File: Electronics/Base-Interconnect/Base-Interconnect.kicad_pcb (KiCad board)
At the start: 2 copper layers, 0 parts

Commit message: Base interconnect and head interconnect in fabrication
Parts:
- added H1: MountingHole_Pad, MountingHole:MountingHole_3.2mm_M3_Pad_Via, F.Cu at (161.7, 45.2)
- added H2: MountingHole_Pad, MountingHole:MountingHole_3.2mm_M3_Pad_Via, F.Cu at (197.8, 48.4)
- added H3: MountingHole_Pad, MountingHole:MountingHole_3.2mm_M3_Pad_Via, F.Cu at (218.6, 84.4)
- added H4: MountingHole_Pad, MountingHole:MountingHole_3.2mm_M3_Pad_Via, F.Cu at (203.3, 117.2)
- added J1: DB9_Male_MountingHoles, STM_Custom_Lib:DSUB-9_Amphenol_LD09S33E4GV00LF-Center, F.Cu at (181.7, 34.0)
- added J2: DB9_Male_MountingHoles, STM_Custom_Lib:DSUB-9_Amphenol_LD09S33E4GV00LF-Center, F.Cu at (213.5, 63.4)
- added J3: DB9_Male_MountingHoles, STM_Custom_Lib:DSUB-9_Amphenol_LD09S33E4GV00LF-Center, F.Cu at (223.1, 105.5)
- added J4: Conn_01x20, STM_Custom_Lib:molex_0526102072, F.Cu at (206.3, 100.6)
- added REF**: OSHW-Symbol_6.7x6mm_SilkScreen, Symbol:OSHW-Symbol_6.7x6mm_SilkScreen, F.Cu at (175.0, 49.0)
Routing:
- net /stepper_A+: track 0.00 -> 76.1 mm, vias 0 -> 1
- net /stepper_A-: track 0.00 -> 74.5 mm, vias 0 -> 1
- net /stepper_B-: track 0.00 -> 72.0 mm, vias 0 -> 1
- net /stepper_B+: track 0.00 -> 71.5 mm, vias 0 -> 1
- net /tunnel_gnd: track 0.00 -> 55.0 mm, vias 0 -> 1
- net /analog_+15V: track 0.00 -> 49.5 mm
- net /tunnel_signal: track 0.00 -> 43.9 mm, vias 0 -> 1
- net /analog_-15V: track 0.00 -> 43.0 mm, vias 0 -> 1
- net /bias: track 0.00 -> 36.6 mm
- net /analog_gnd: track 0.00 -> 23.1 mm, vias 0 -> 19
- net /piezo_y+: track 0.00 -> 19.9 mm, vias 0 -> 1
- net /piezo_x+: track 0.00 -> 19.1 mm, vias 0 -> 1
- net /piezo_x-: track 0.00 -> 13.9 mm
- net /piezo_y-: track 0.00 -> 10.9 mm
- added copper zone on B.Cu, net /analog_gnd
- added copper zone on F.Cu, net /analog_gnd
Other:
- board outline added: 66.5 x 101.6 mm
- board text added: "STM Base Interconnect V1"
- board text added: "©mrkenhoff 2020"

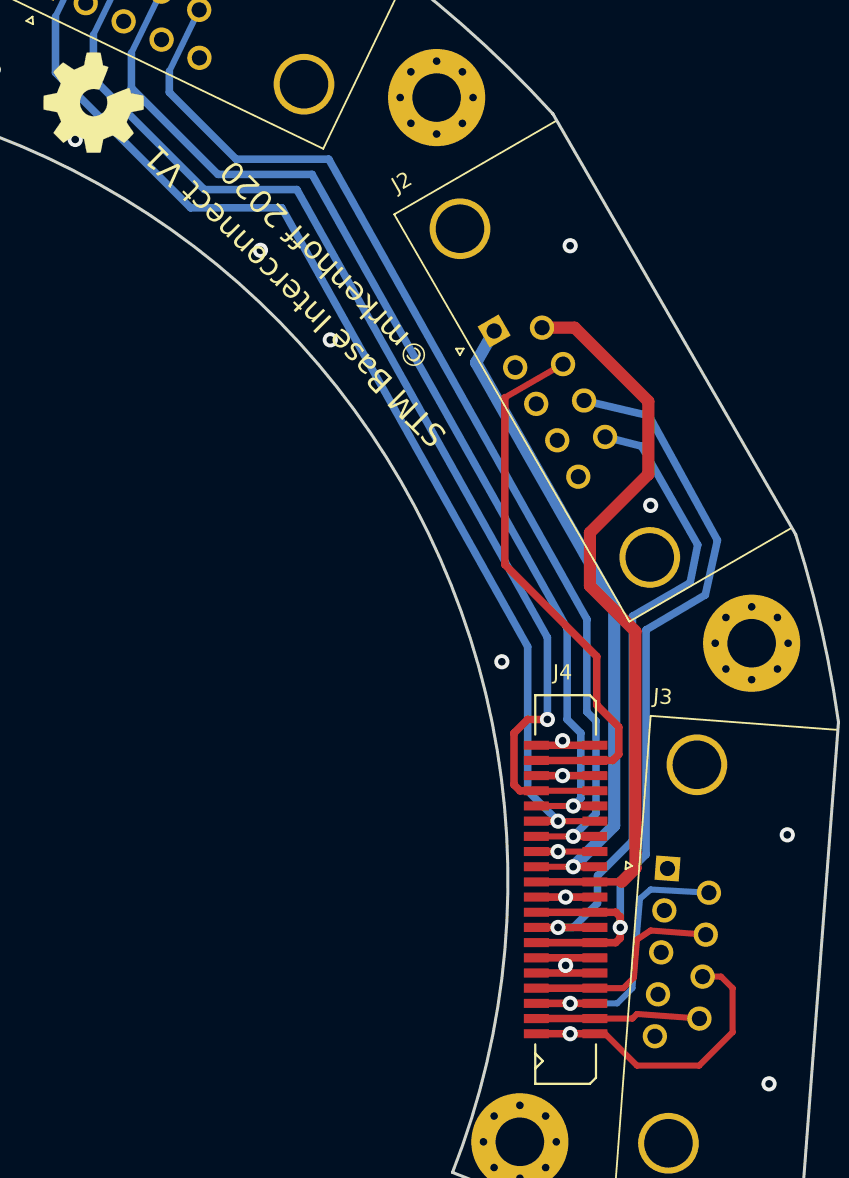
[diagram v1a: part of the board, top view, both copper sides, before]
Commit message: Added sample-bias interconnect and base interconnect V2
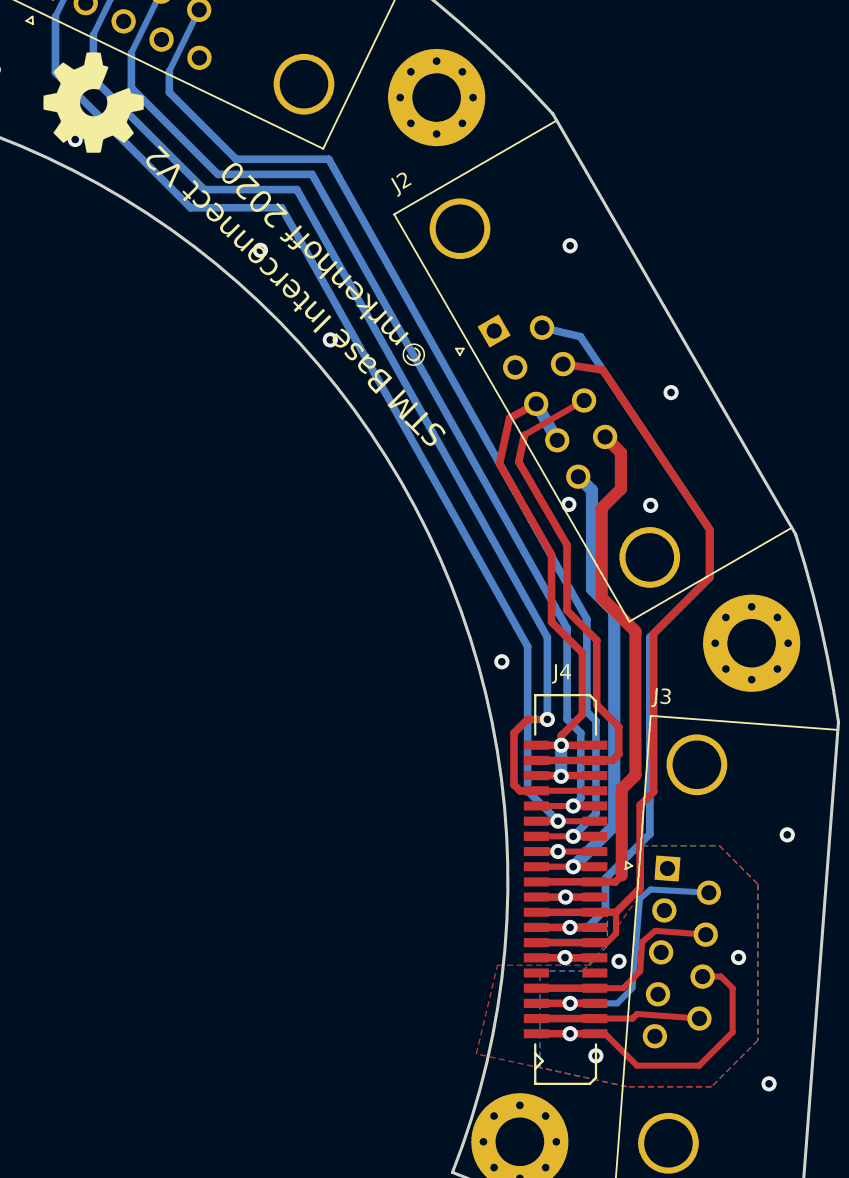
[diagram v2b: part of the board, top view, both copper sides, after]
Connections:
- J1 pad 1: /stepper_shield -> Net-(J1-Pad1)
- J1 pad 2: /stepper_shield -> Net-(J1-Pad2)
- J1 pad 3: /stepper_shield -> Net-(J1-Pad3)
- J1 pad 4: /stepper_shield -> Net-(J1-Pad4)
- J1 pad 5: /stepper_shield -> Net-(J1-Pad5)
- J1 pad 6: /stepper_A+ -> /stepper_B-
- J1 pad 7: /stepper_A- -> /stepper_B+
- J1 pad 8: /stepper_B+ -> /stepper_A-
- J1 pad 9: /stepper_B- -> /stepper_A+
- J2 pad 1: /analog_-15V -> /analog_gnd
- J2 pad 3: /analog_gnd -> /bias_gnd
- J2 pad 4: /analog_gnd -> /bias_gnd
- J2 pad 5: /analog_gnd -> /analog_-15V
- J2 pad 6: /analog_+15V -> /tunnel_signal
- J2 pad 7: /bias -> /tunnel_gnd
- J2 pad 8: /tunnel_gnd -> /bias
- J2 pad 9: /tunnel_signal -> /analog_+15V
- J3 pad 1: /analog_gnd -> /piezo_gnd
- J3 pad 2: /analog_gnd -> /piezo_gnd
- J3 pad 3: /analog_gnd -> /piezo_gnd
- J3 pad 4: /analog_gnd -> /piezo_gnd
- J3 pad 5: /analog_gnd -> /piezo_gnd
- J3 pad 6: /piezo_x+ -> /piezo_y-
- J3 pad 7: /piezo_x- -> /piezo_y+
- J3 pad 8: /piezo_y+ -> /piezo_x-
- J3 pad 9: /piezo_y- -> /piezo_x+
- J4 pad 1: /piezo_y+ -> /piezo_x-
- J4 pad 14: /stepper_B- -> /stepper_A+
- J4 pad 15: /stepper_A+ -> /stepper_B-
- J4 pad 16: /stepper_B+ -> /stepper_A-
- J4 pad 17: /stepper_A- -> /stepper_B+
- J4 pad 18: /analog_gnd -> /bias_gnd
- J4 pad 2: /piezo_y- -> /piezo_x+
- J4 pad 20: /analog_gnd -> /bias_gnd
- J4 pad 3: /piezo_x+ -> /piezo_y-
- J4 pad 4: /piezo_x- -> /piezo_y+
- J4 pad 5: /analog_gnd -> /piezo_gnd
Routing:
- net /bias_gnd: track 0.00 -> 38.5 mm, vias 0 -> 2
- net /analog_+15V: track 49.5 -> 36.9 mm
- net /analog_gnd: track 23.1 -> 11.5 mm
- net /analog_-15V: track 43.0 -> 31.6 mm
- net /tunnel_signal: track 43.9 -> 52.4 mm
- net /piezo_y-: track 10.9 -> 19.1 mm, vias 0 -> 1
- net /piezo_x+: track 19.1 -> 10.9 mm, vias 1 -> 0
- net /piezo_y+: track 19.9 -> 13.7 mm, vias 1 -> 0
- net /piezo_x-: track 13.9 -> 19.9 mm, vias 0 -> 1
- net /stepper_B-: track 72.0 -> 76.1 mm
- net /stepper_A+: track 76.1 -> 72.0 mm
- net /bias: track 36.6 -> 33.5 mm
- net /stepper_B+: track 71.5 -> 74.5 mm
- net /stepper_A-: track 74.5 -> 71.5 mm
- net /tunnel_gnd: track 55.0 -> 55.2 mm, vias 1 -> 0
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- added copper zone on B.Cu, net /piezo_gnd
- added copper zone on F.Cu, net /piezo_gnd
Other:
- board text added: "STM Base Interconnect V2"
- board text removed: "STM Base Interconnect V1"
